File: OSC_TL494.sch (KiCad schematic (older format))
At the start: 9 parts, among them IC1 TL494

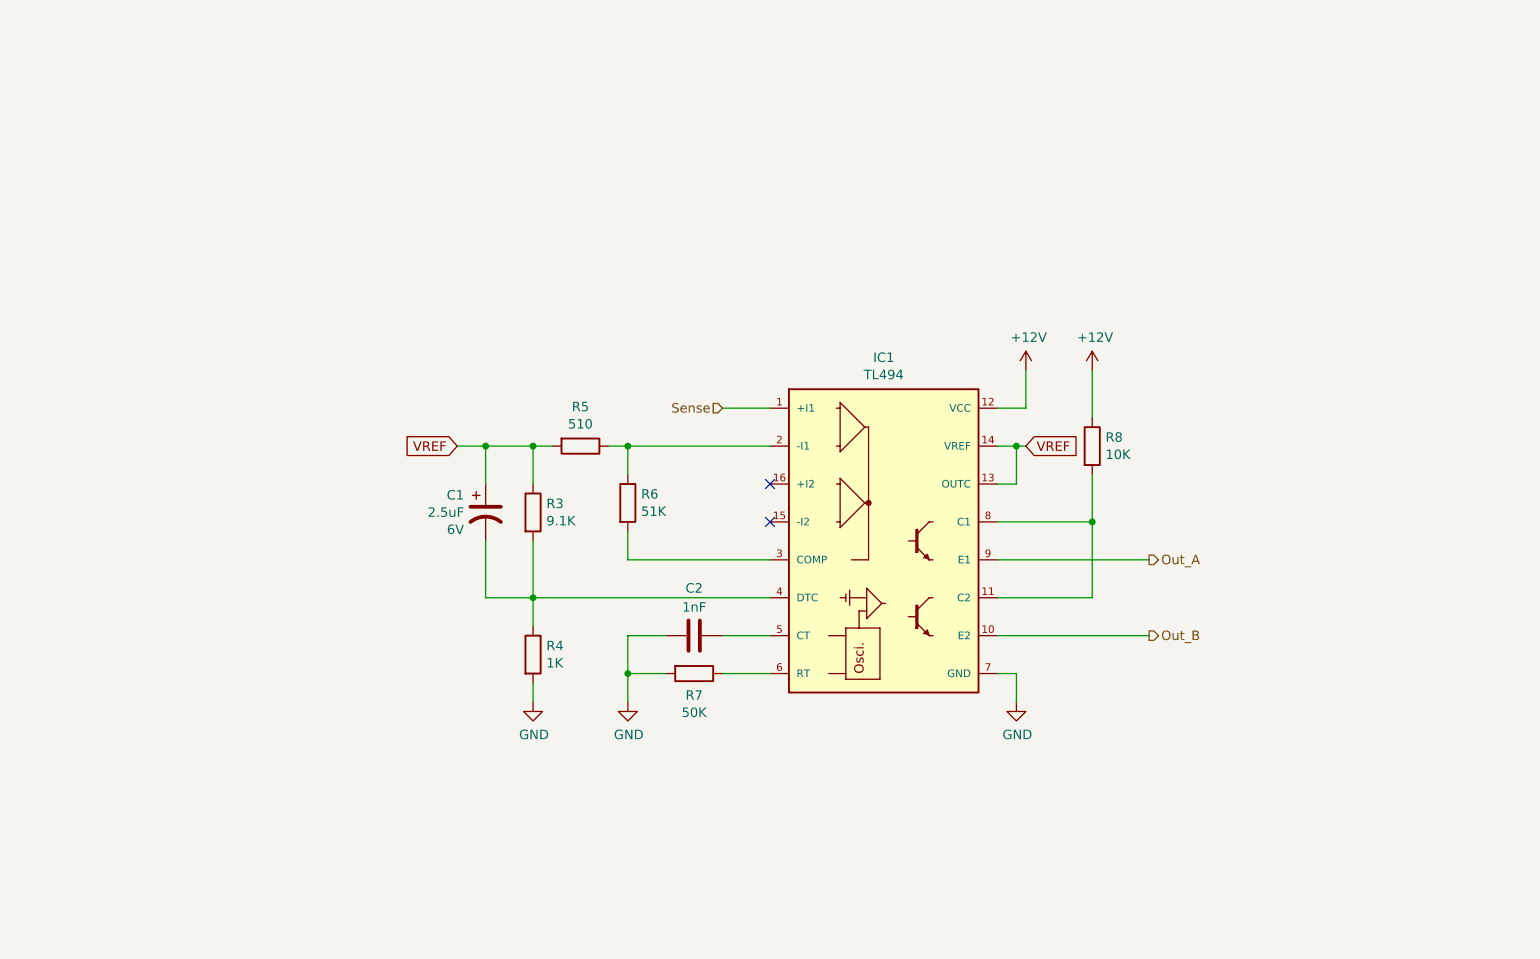
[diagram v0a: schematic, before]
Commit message: separando el modulo de oscilacion en otra  placa
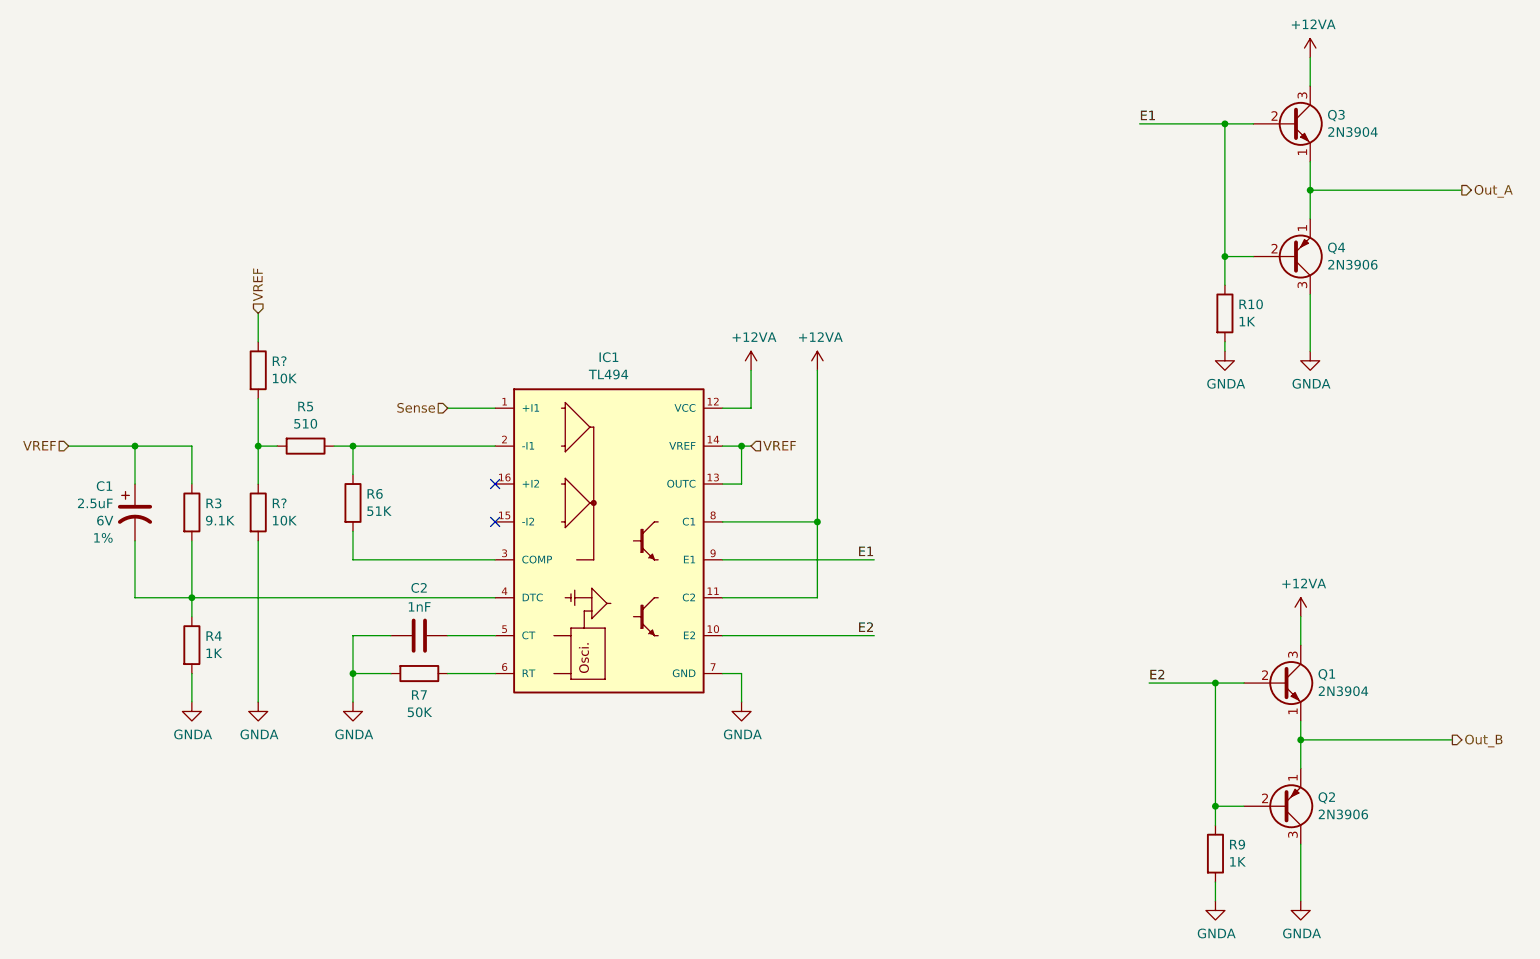
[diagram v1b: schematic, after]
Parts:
- removed R8: 10K, Resistor_THT:R_Axial_DIN0207_L6.3mm_D2.5mm_P10.16mm_Horizontal, symbol Device:R
- added Q1, Q3: 2N3904, Package_TO_SOT_THT:TO-92L_HandSolder, symbol Device:Q_NPN_EBC
- added Q2, Q4: 2N3906, Package_TO_SOT_THT:TO-92L_HandSolder, symbol Device:Q_PNP_EBC
- added R10, R9: 1K, Resistor_THT:R_Axial_DIN0207_L6.3mm_D2.5mm_P10.16mm_Horizontal, symbol Device:R
- added R? (x2): 10K, Resistor_THT:R_Axial_DIN0207_L6.3mm_D2.5mm_P10.16mm_Horizontal, symbol Device:R
- C1: Campo4 6V -> (none); Campo7 (none) -> 1%; V (none) -> 6V
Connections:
- net +12V is gone; now on net +12VA: IC1.12 (VCC)
- net Out_A: now also Q3.1 (E), Q4.1 (E); no longer IC1.9 (E1)
- net Out_B: now also Q1.1 (E), Q2.1 (E); no longer IC1.10 (E2)
- net VREF: now also R?.1; no longer R5.2
- net +12VA: now reaches IC1.11 (C2), IC1.8 (C1)
- net +12VA: now also Q1.3 (C), Q3.3 (C)
- net GND renamed GNDA
- net GNDA: now also Q2.3 (C), Q4.3 (C), R10.2, R9.2, R?.2
- new net: R5.2, R?.1, R?.2
- new net E1: IC1.9 (E1), Q3.2 (B), Q4.2 (B), R10.1
- new net E2: IC1.10 (E2), Q1.2 (B), Q2.2 (B), R9.1
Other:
- moved on the sheet: C1, C2, IC1, R3, R4, R5, R6, R7
